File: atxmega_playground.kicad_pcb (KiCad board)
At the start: 2 copper layers, 101.3 x 96.5 mm, 115 parts, among them CON1 AVR-PDI-6, IC1 ATXMEGA32A4U-A, P1 USB_OTG, P2 CONN_01X02, P3 CONN_01X02, P4 CONN_01X06, P5 CONN_01X03, P6 CONN_01X04, P7 CONN_01X04, P8 CONN_01X07, Q1 PMOS, Q2 NMOS, Q3 NMOS, Q4 NMOS, U1 NCP346, U10 WS2812B, U11 WS2812B, U12 74HC595_F, U13 74HC595_F, U14 AT25SF041, U15 REF195, U16 AD7708, U17 MPXH6101A, U18 LM35, U2 LM3940, U3 ADM3315E, U4 HI-3110, U5 INA139, U6 WS2812B, U7 SN65220, U8 WS2812B, Y1 16MHz, Y2 32.768kHz

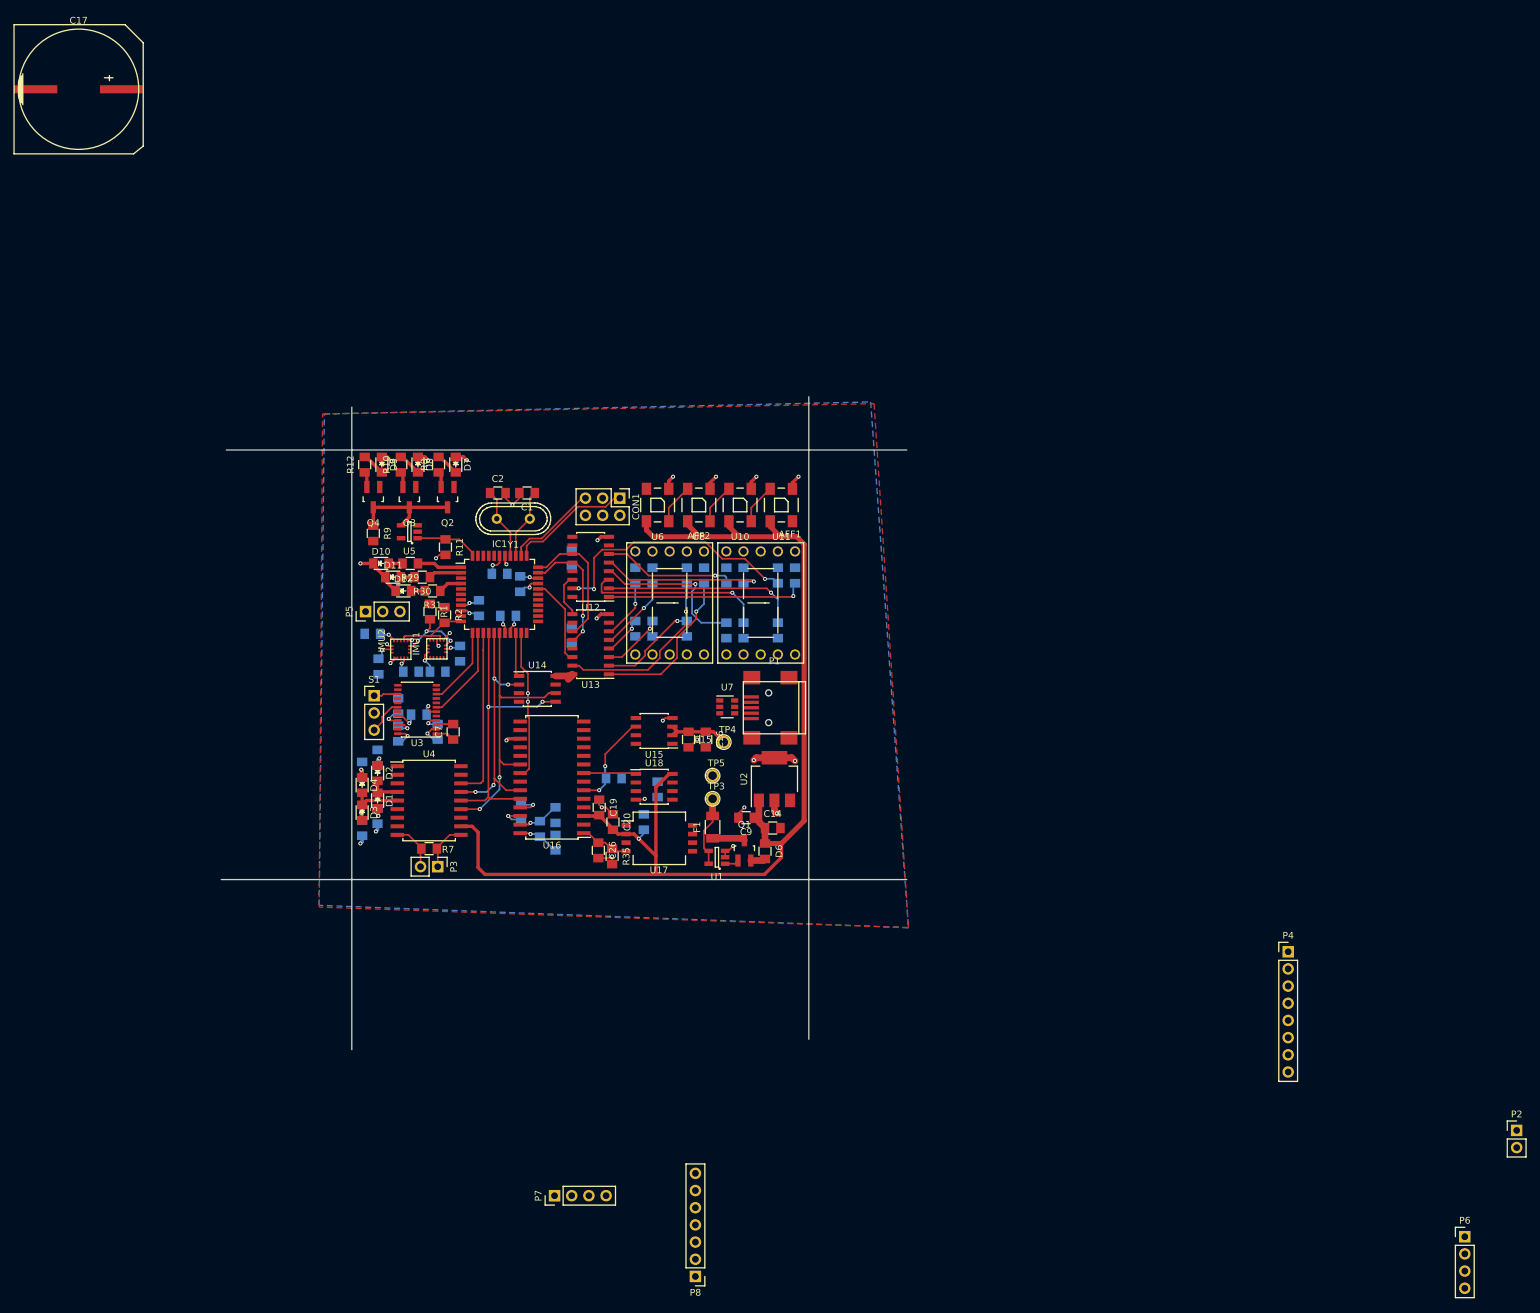
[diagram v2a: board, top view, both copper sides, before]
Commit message: Initial layout complete, no DRC errors or unconnected tracks
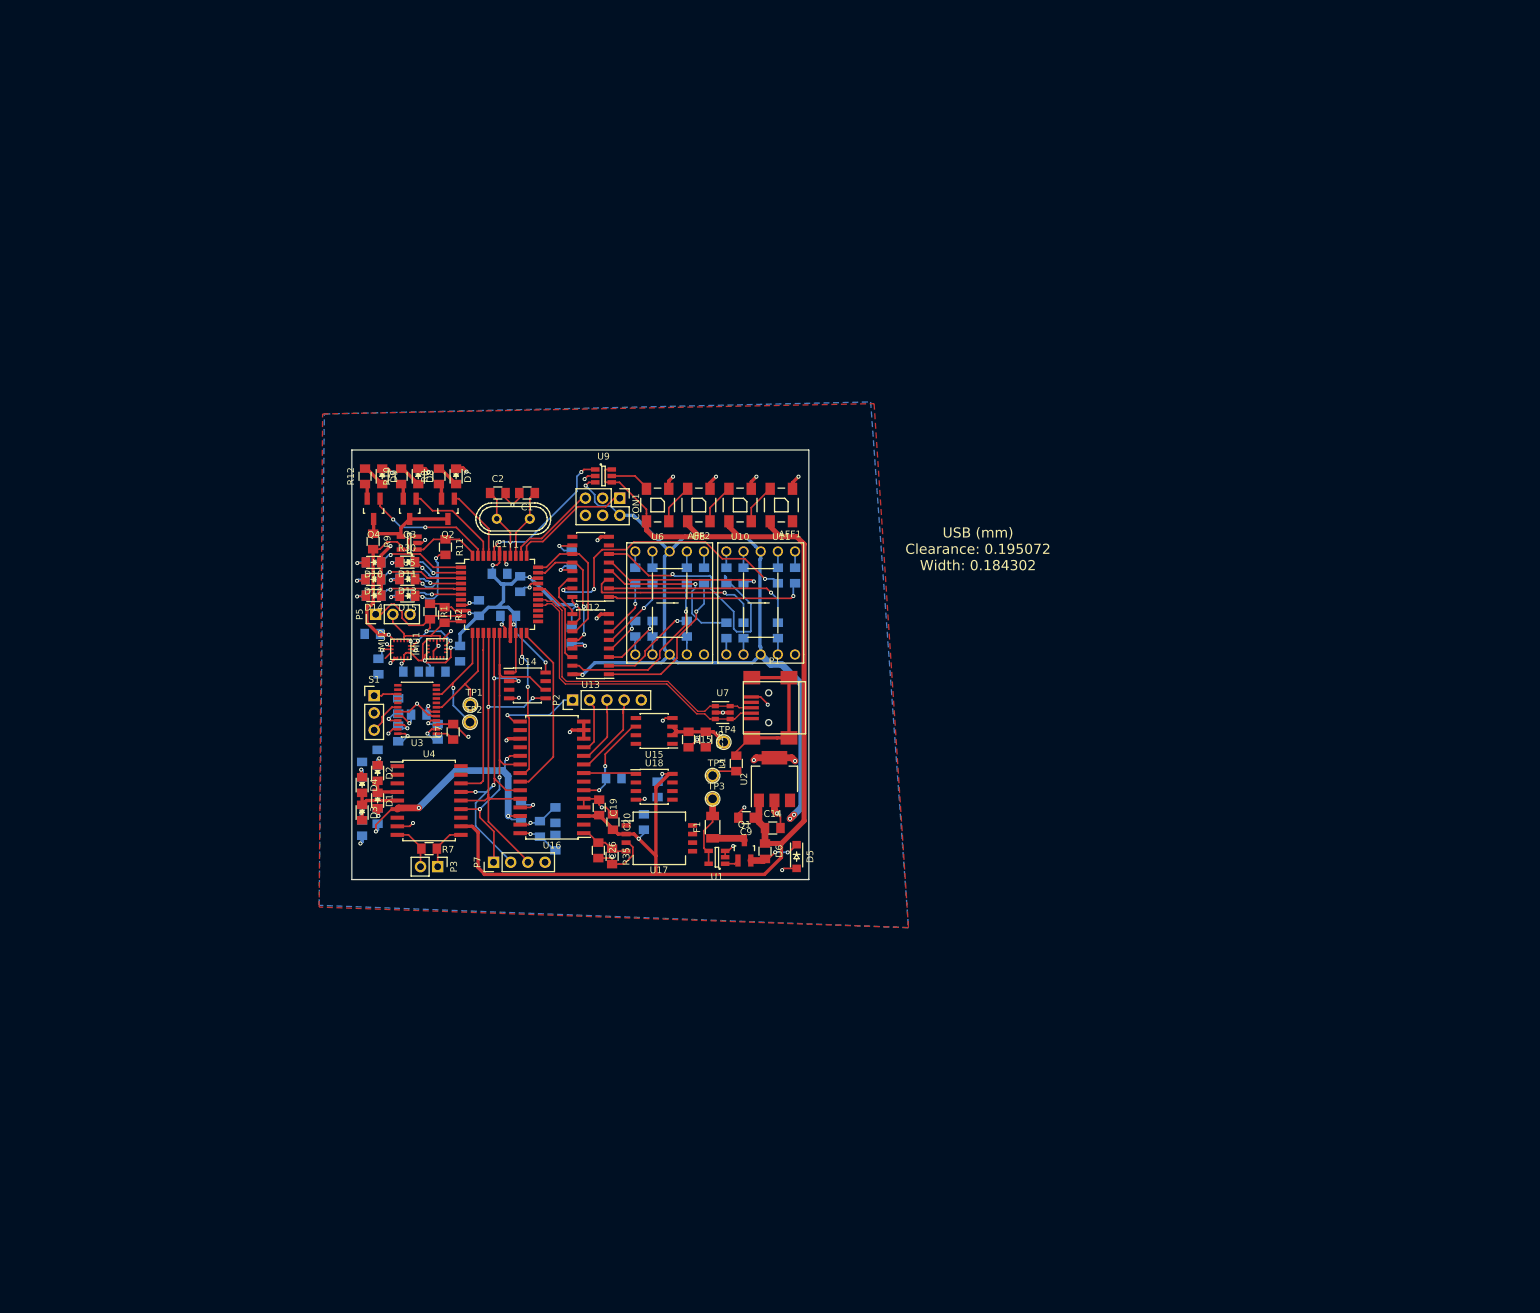
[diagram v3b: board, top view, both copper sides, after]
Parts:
- removed C17: 1uF, atxmega:c_elec_18x21.5
- removed P4: CONN_01X06, Pin_Headers:Pin_Header_Straight_1x08_Pitch2.54mm
- removed P6: CONN_01X04, Pin_Headers:Pin_Header_Straight_1x04_Pitch2.54mm
- removed P8: CONN_01X07, Pin_Headers:Pin_Header_Straight_1x07_Pitch2.54mm
- added D13: LED, atxmega:LED_0805, F.Cu at (87.5, 45.5)
- added D14: LED, atxmega:LED_0805, F.Cu at (82.5, 47.9)
- added D15: LED, atxmega:LED_0805, F.Cu at (87.5, 48.0)
- added D5: D_Zener, atxmega:SOD-123, F.Cu at (145.0, 86.5)
- added L1: Ferrite_Bead, atxmega:R_0805, F.Cu at (136.1, 72.7)
- added R32: R, atxmega:R_0805, B.Cu at (87.4, 45.4)
- added R33: R, atxmega:R_0805, B.Cu at (82.5, 48.0)
- added R34: R, atxmega:R_0805, B.Cu at (87.4, 48.0)
- added TP1: TEST, atxmega:TESTPOINT, F.Cu at (96.8, 64.1)
- added TP2: TEST, atxmega:TESTPOINT, F.Cu at (96.7, 66.6)
- added U9: PI4ULS5V201, atxmega:SOT-23-6, F.Cu at (116.5, 30.3)
- P2: value CONN_01X02 -> CONN_01X05; footprint Pin_Headers:Pin_Header_Straight_1x02_Pitch2.54mm -> Pin_Headers:Pin_Header_Straight_1x05_Pitch2.54mm
- R29, R30, R31: moved to B.Cu
- moved P2 153.4 mm to (111.9, 63.4), turned to 90 degrees
- moved P7 50.1 mm to (100.2, 87.4)
- moved R31 8.90 mm to (82.4, 45.5)
- moved R29 5.39 mm to (82.5, 43.0)
- moved D12 4.76 mm to (82.4, 45.5), turned to 180 degrees
- moved R30 3.16 mm to (87.4, 43.0)
- moved D11 3.05 mm to (87.5, 43.0), turned to 180 degrees
- moved D7 1.73 mm to (94.7, 30.3)
- moved R10 1.73 mm to (86.5, 30.3)
- moved D8 1.73 mm to (89.1, 30.3)
- moved D9 1.73 mm to (83.7, 30.3)
- moved R12 1.73 mm to (81.2, 30.3)
- moved R8 1.73 mm to (92.1, 30.3)
- moved Q2 1.73 mm to (93.5, 35.1)
- moved Q3 1.73 mm to (87.8, 35.1)
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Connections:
- IC1 pad 22: /PD_3 -> /ADC_RDY
- IC1 pad 23: /GPIO5 -> (no net)
- IC1 pad 24: /IMU_INT1 -> (no net)
- IC1 pad 25: /IMU_INT2 -> (no net)
- IC1 pad 28: /GPIO1 -> (no net)
- IC1 pad 3: (no net) -> /LED3
- IC1 pad 4: /LED3 -> /LED4
- IC1 pad 40: (no net) -> /LED_DIN_3.3V
- IC1 pad 41: /MC_ADC1 -> /PD_1
- IC1 pad 42: /MC_ADC2 -> /PD_2
- IC1 pad 43: /MC_ADC3 -> /PD_3
- IC1 pad 5: (no net) -> /LED5
- IC1 pad 6: (no net) -> /LED6
- IMU2 pad 11: /IMU_INT1 -> (no net)
- IMU2 pad 9: /IMU_INT2 -> (no net)
- P2 pad 1: +5V -> /ADC4
- P2 pad 2: GND -> /ADC3
- Q2 pad 2: (no net) -> /PD_1
- Q3 pad 2: (no net) -> /PD_2
- U16 pad 19: (no net) -> +3V3
- U16 pad 2: /ADC6 -> (no net)
- U16 pad 22: (no net) -> /ADC_RDY
- U16 pad 7: /ADC5 -> (no net)
- U6 pad 4: (no net) -> /LED_DIN_5V
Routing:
- net +3V3: track 35.0 -> 298.8 mm, vias 11 -> 21
- net GND: track 79.6 -> 148.1 mm, vias 33 -> 47
- net /USB_D-: track 0.00 -> 44.8 mm
- net /USB_D+: track 0.00 -> 44.5 mm
- net /ADC_RDY: track 0.00 -> 26.4 mm
- net Net-(L1-Pad2): track 0.00 -> 23.6 mm
- net /LED_DIN_3.3V: track 0.00 -> 22.3 mm, vias 0 -> 2
- net Net-(R21-Pad2): track 19.7 -> 39.6 mm
- net /PD_3: track 0.00 -> 19.7 mm, vias 0 -> 2
- net /SPIC_MISO: track 37.8 -> 54.8 mm
- net /SDA: track 10.6 -> 26.2 mm
- net +5V: track 185.1 -> 200.4 mm, vias 1 -> 2
- net /PD_2: track 0.00 -> 14.7 mm
- net /ADC4: track 0.00 -> 12.8 mm, vias 0 -> 1
- net /ADC1: track 0.00 -> 12.7 mm
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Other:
- board size 101.3 x 96.5 mm -> 67.6 x 63.5 mm
- net class USB added: clearance 0.1524, trace_width 0.1524, via_dia 0.6, via_drill 0.3048
- rule trace_min: 0.2 -> 0.1524
- board text added: "USB (mm) Clearance: 0.195072 Width: 0.184302"
